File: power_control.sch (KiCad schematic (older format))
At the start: 80 parts, among them J26 Conn_01x02, J27 Conn_01x02, J28 Conn_01x02, J29 Conn_01x02, J30 Conn_01x02, J31 Conn_01x02, J32 Conn_01x02, J33 Conn_01x02, U10 L6203, U11 L6203, U12 L6203, U5 L6203, U6 L6203, U7 L6203, U8 L6203, U9 L6203

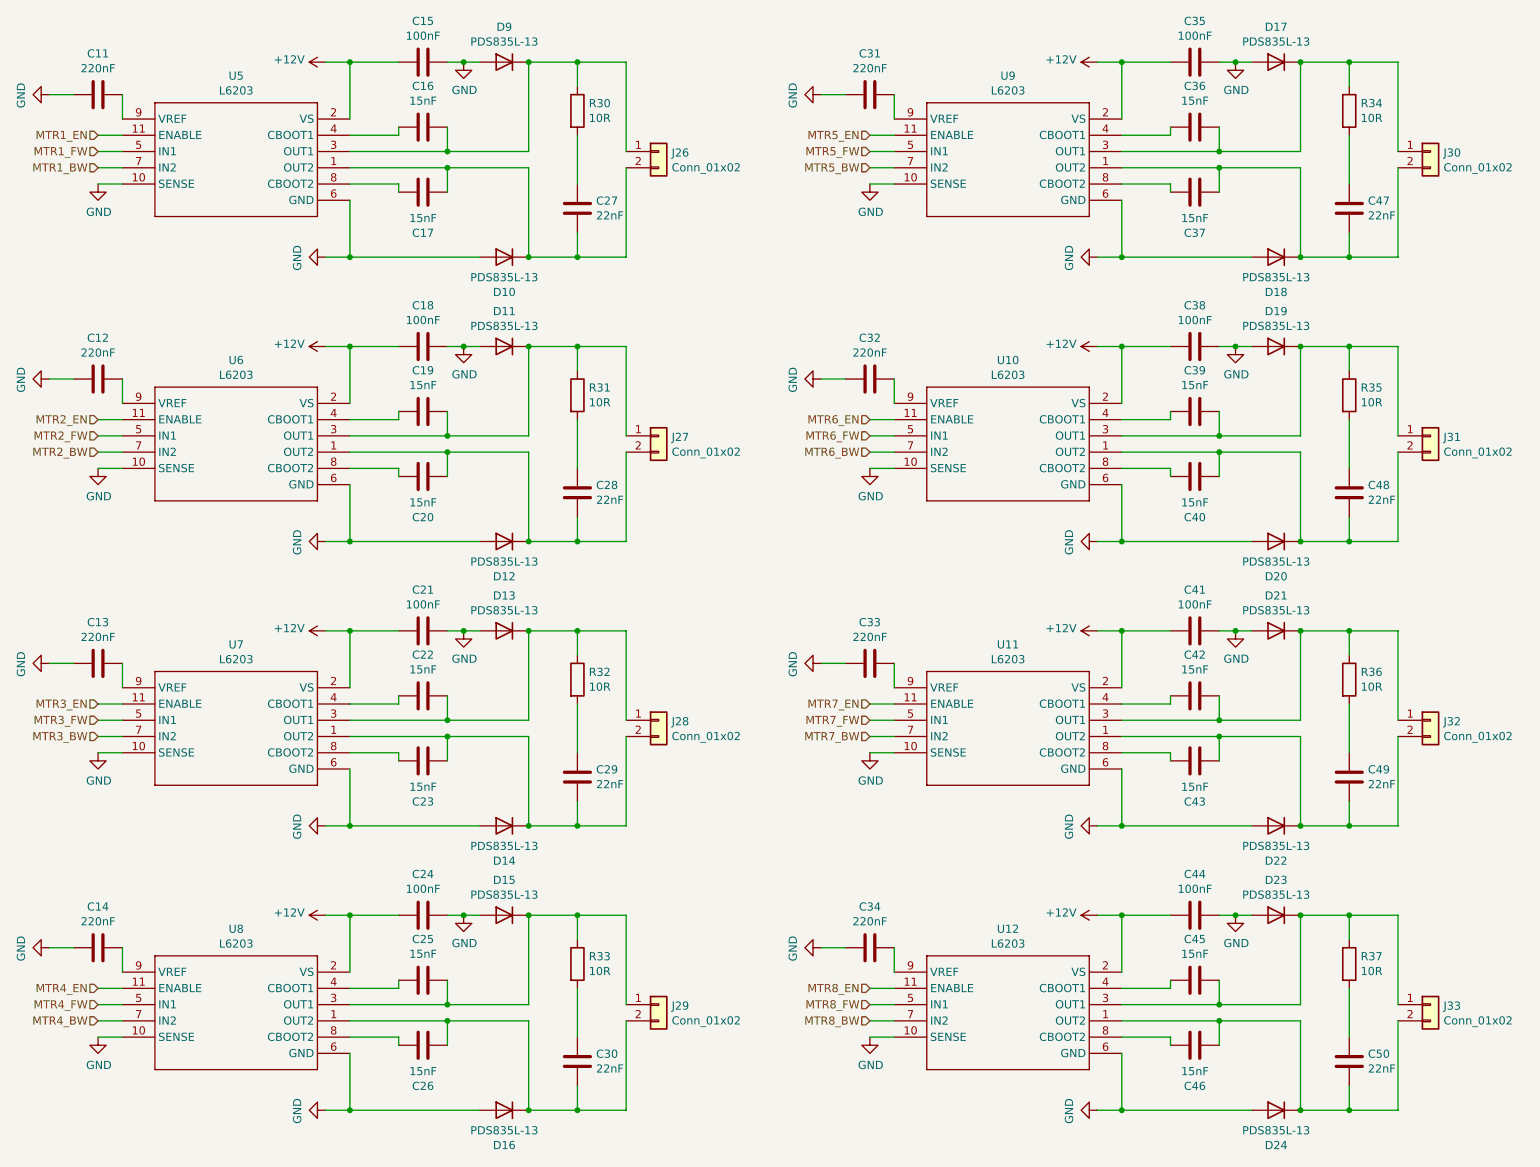
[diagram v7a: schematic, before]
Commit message: Changed "out of stock" references.
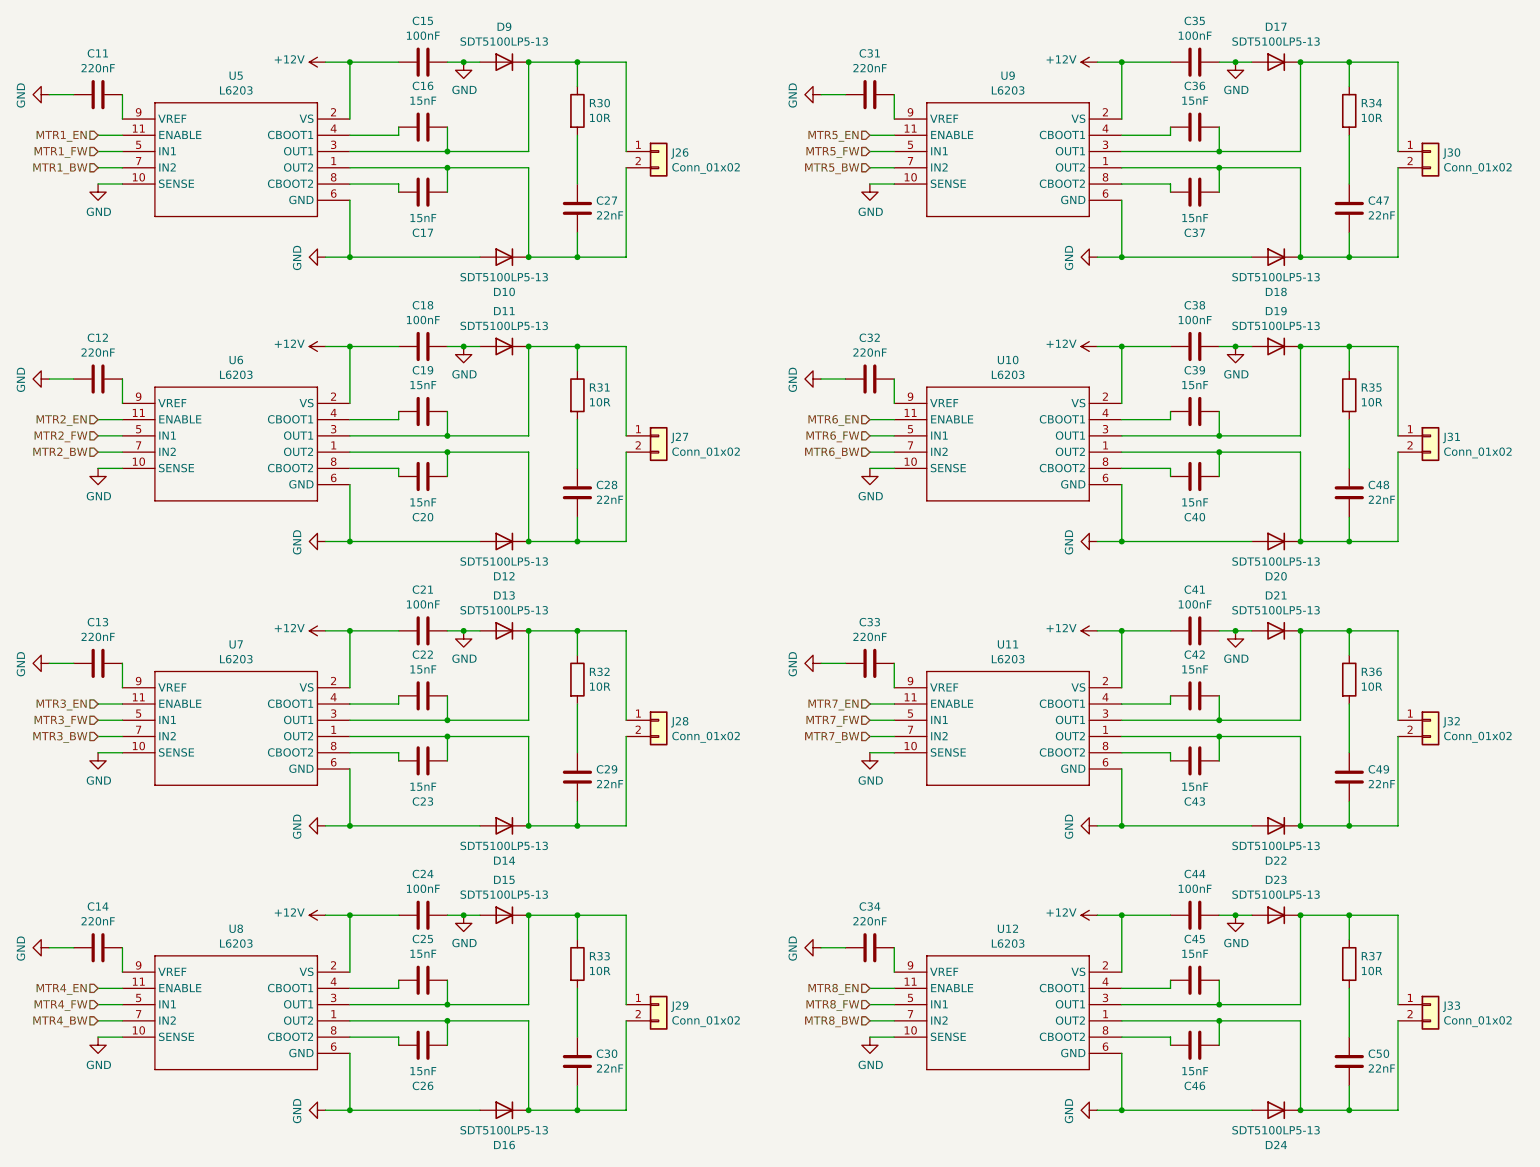
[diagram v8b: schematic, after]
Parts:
- C16, C17, C19, C20, C22, C23, C25, C26, C36, C37, C39, C40, C42, C43, C45, C46: manf# C0603C153M4RECTU -> 885012206041
- D10, D11, D12, D13, D14, D15, D16, D17, D18, D19, D20, D21, D22, D23, D24, D9: value PDS835L-13 -> SDT5100LP5-13; manf# PDS835L-13 -> SDT5100LP5-13
